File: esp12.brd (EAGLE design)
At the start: 49.7 x 49.8 mm, 30 parts, among them IC1 117\33

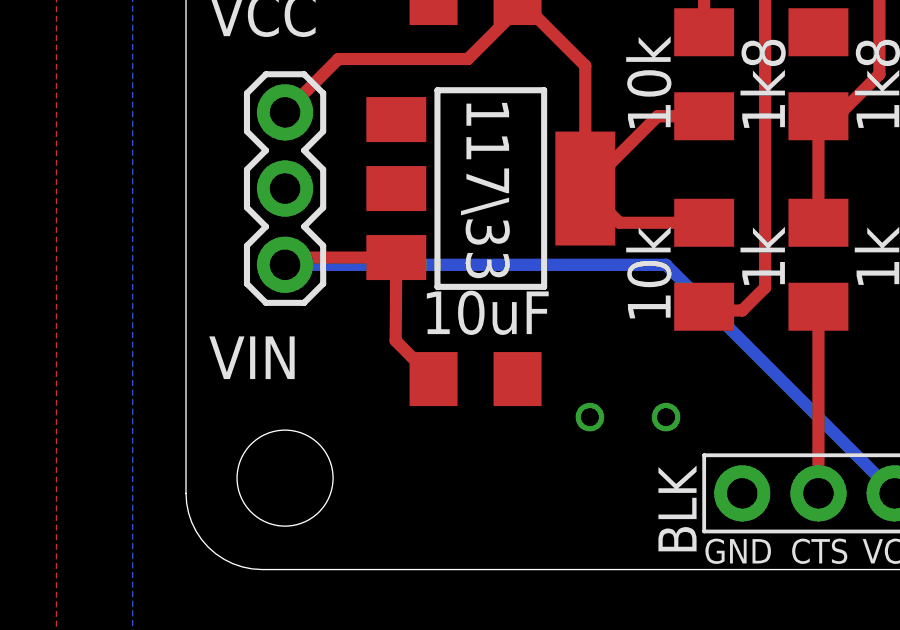
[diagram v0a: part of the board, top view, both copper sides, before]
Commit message: 100nF because of regulator
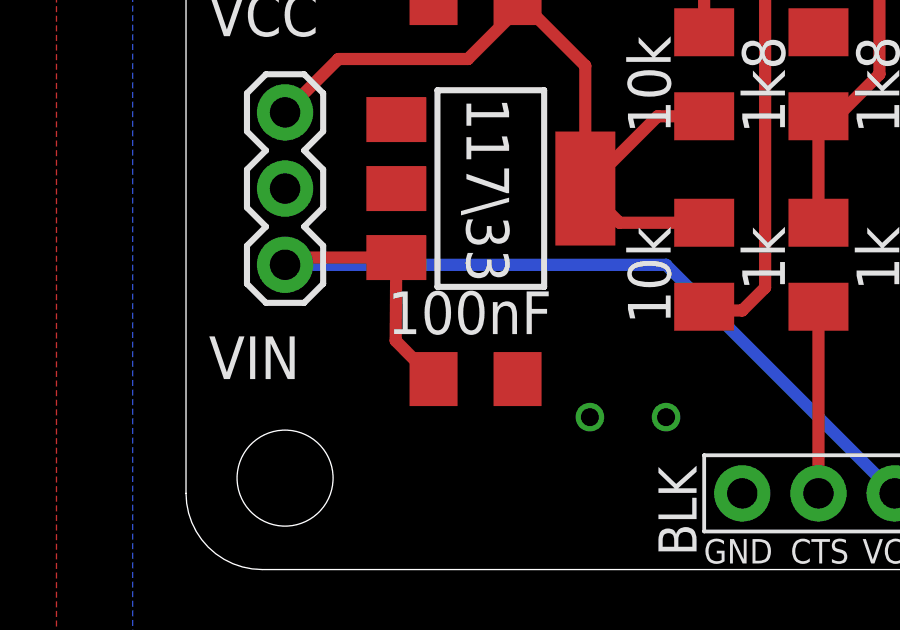
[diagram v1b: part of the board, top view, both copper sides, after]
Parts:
- C1: value 10uF -> 100nF
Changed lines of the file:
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@@
 <attribute name="VALUE" x="8.5852" y="15.748" size="1.4224" layer="25" font="vector" rot="SR270"/>
 </element>
-<element name="C1" library="resistor" package="C1206" value="10uF" x="8.89" y="6.35" smashed="yes" rot="R180">
+<element name="C1" library="resistor" package="C1206" value="100nF" x="8.89" y="6.35" smashed="yes" rot="R180">
 <attribute name="VALUE" x="11.43" y="9.271" size="1.4224" layer="25" font="vector" rot="R180"/>
 </element>
